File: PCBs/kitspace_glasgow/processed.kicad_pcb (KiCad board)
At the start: 4 copper layers, 80 x 49 mm, 267 parts, among them J1 USB_C_USB2.0, J10 AUX, J2 IDC-Header_2x10_P2.54mm, J3 IDC-Header_2x10_P2.54mm, J4 Conn_01x02, J5 PinHeader_2x22_P1.27mm, J6 Conn_01x08, J7 Conn_01x08, J8 Conn_01x08, J9 Conn_01x08, SW1 RST, U1 CY7C68013A-56LTX, U10 SN74LVC1T45DCKR, U11 SN74LVC1T45DCKR, U12 INA233, U13 DAC081C081CIMK, U14 TPS73101DBV, U15 TPD3S014, U16 SN74LVC1T45DCKR, U17 SN74LVC1T45DCKR, U18 SN74LVC1T45DCKR, U19 PCA6408APW, U2 CAT24M01X, U20 DAC081C081CIMK, U21 INA233, U22 SN74LVC1T45DCKR, U23 SN74LVC1T45DCKR, U24 SN74LVC1T45DCKR, U25 SN74LVC1T45DCKR, U26 SN74LVC1T45DCKR, U27 SN74LVC1T45DCKR, U28 SN74LVC1T45DCKR, U29 SN74LVC1T45DCKR, U3 BL24C256A-SFRC, U30 ICE40HX8K-BG121, U31 TPS73101DBV, U32 SN74LVC1T45DCKR, U36 TLV73312PQDRVR, U4 SN74LVC1T45DCKR, U5 PCA6408APW, U6 SN74LVC1T45DCKR, U7 APX811-40UG-7, U8 TLV75533PDRVR, U9 SN74LVC1T45DCKR, Y1 24M

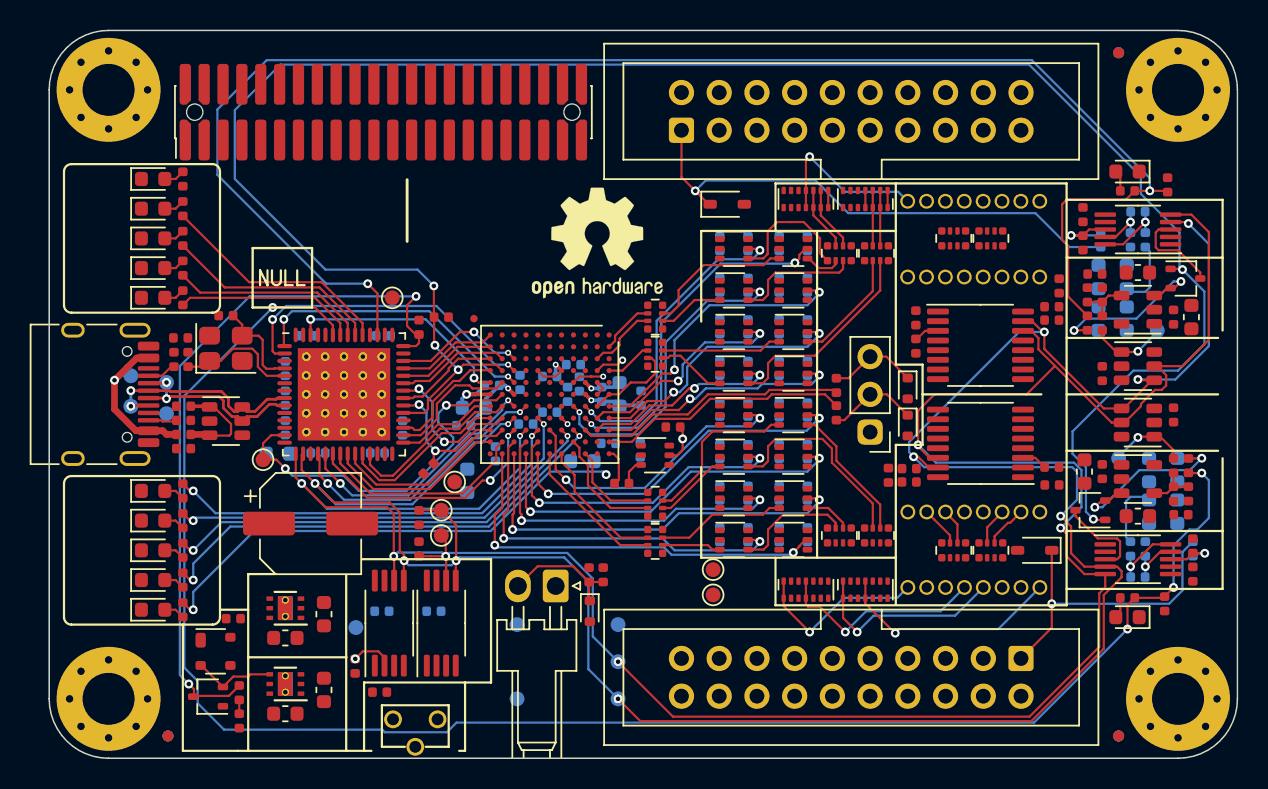
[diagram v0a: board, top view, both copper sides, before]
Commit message: recheck all circuits and clean up fill zone by rerouting the nets using freerouting and manually
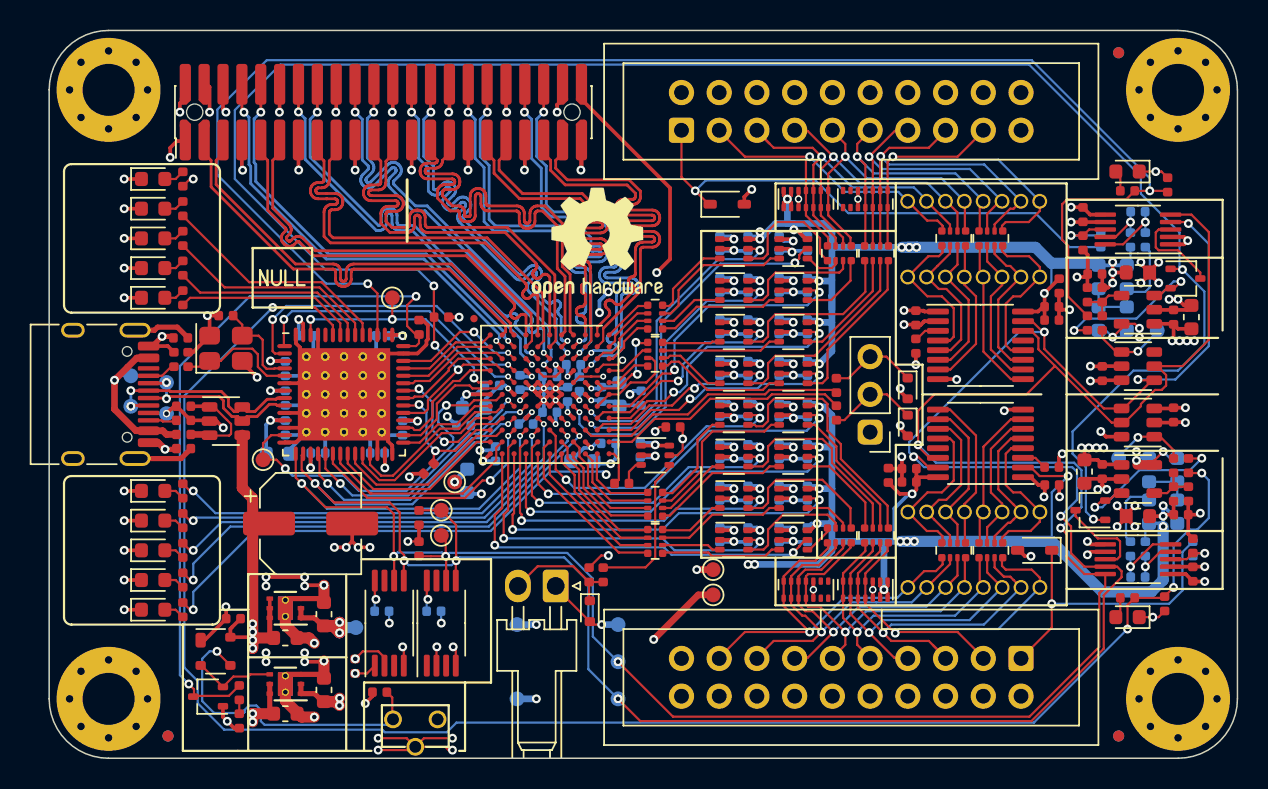
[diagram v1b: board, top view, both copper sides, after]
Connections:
- C1 pad 1: (no net) -> +3V3
- C1 pad 2: (no net) -> GND
- C10 pad 1: (no net) -> +3V3
- C10 pad 2: (no net) -> GND
- C11 pad 2: (no net) -> GND
- C12 pad 2: (no net) -> GND
- C13 pad 1: (no net) -> /SHLD
- C13 pad 2: (no net) -> GND
- C14 pad 1: (no net) -> +1V2
- C14 pad 2: (no net) -> GND
- C15 pad 1: (no net) -> +3V3
- C15 pad 2: (no net) -> GND
- C16 pad 1: (no net) -> +5V
- C16 pad 2: (no net) -> GND
- C17 pad 1: (no net) -> +3V3
- C17 pad 2: (no net) -> GND
- C18 pad 1: (no net) -> +1V2
- C18 pad 2: (no net) -> GND
- C19 pad 1: (no net) -> +3V3
- C19 pad 2: (no net) -> GND
- C2 pad 1: (no net) -> +3V3
- C2 pad 2: (no net) -> GND
- C20 pad 1: (no net) -> +3V3
- C20 pad 2: (no net) -> GND
- C21 pad 1: (no net) -> +3V3
- C21 pad 2: (no net) -> GND
- C22 pad 1: (no net) -> +3V3
- C22 pad 2: (no net) -> GND
- C23 pad 1: (no net) -> +3V3
- C23 pad 2: (no net) -> GND
- C24 pad 1: (no net) -> +1V2
- C24 pad 2: (no net) -> GND
- C25 pad 1: (no net) -> +1V2
- C25 pad 2: (no net) -> GND
- C26 pad 1: (no net) -> GND
- C26 pad 2: (no net) -> +5V
- C27 pad 1: (no net) -> +1V2
- C27 pad 2: (no net) -> GND
- C28 pad 1: (no net) -> +3V3
- C28 pad 2: (no net) -> GND
- C29 pad 1: (no net) -> /IO_Banks/VIOB
- C29 pad 2: (no net) -> GND
- C3 pad 1: (no net) -> +3V3
- C3 pad 2: (no net) -> GND
- C30 pad 1: (no net) -> +3V3
- C30 pad 2: (no net) -> GND
- C31 pad 1: (no net) -> +5V
- C31 pad 2: (no net) -> GND
- C32 pad 1: (no net) -> +3V3
- C32 pad 2: (no net) -> GND
- C33 pad 2: (no net) -> GND
- C34 pad 1: (no net) -> +3V3
- C34 pad 2: (no net) -> GND
- C35 pad 1: (no net) -> +3V3
- C35 pad 2: (no net) -> GND
- C36 pad 1: (no net) -> +3V3
- C36 pad 2: (no net) -> GND
- C37 pad 1: (no net) -> +3V3
- C37 pad 2: (no net) -> GND
- C38 pad 1: (no net) -> /IO_Banks/VIOA
- C38 pad 2: (no net) -> GND
- C39 pad 1: (no net) -> /IO_Banks/VIOA
- C39 pad 2: (no net) -> GND
- C4 pad 1: (no net) -> +3V3
- C4 pad 2: (no net) -> GND
- C40 pad 1: (no net) -> /IO_Banks/VIOA
- C40 pad 2: (no net) -> GND
- C41 pad 1: (no net) -> /IO_Banks/VIOA
- C41 pad 2: (no net) -> GND
- C42 pad 1: (no net) -> +3V3
- C42 pad 2: (no net) -> GND
- C43 pad 1: (no net) -> +3V3
- C43 pad 2: (no net) -> GND
- C45 pad 1: (no net) -> +5V
- C45 pad 2: (no net) -> GND
- C46 pad 1: (no net) -> /IO_Banks/VIOB
- C46 pad 2: (no net) -> GND
- C47 pad 1: (no net) -> +3V3
- C47 pad 2: (no net) -> GND
- C48 pad 1: (no net) -> +3V3
- C48 pad 2: (no net) -> GND
- C49 pad 1: (no net) -> /IO_Banks/VIOA
- C49 pad 2: (no net) -> GND
- C5 pad 1: (no net) -> +3V3
- C5 pad 2: (no net) -> GND
- C50 pad 1: (no net) -> /IO_Banks/VIOA
- C50 pad 2: (no net) -> GND
- C51 pad 1: (no net) -> /IO_Banks/VIOA
- C51 pad 2: (no net) -> GND
- C52 pad 1: (no net) -> /IO_Banks/VIOA
- C52 pad 2: (no net) -> GND
- C53 pad 1: (no net) -> /IO_Banks/VIOB
- C53 pad 2: (no net) -> GND
- C54 pad 1: (no net) -> /IO_Banks/VIOA
- C54 pad 2: (no net) -> GND
- C55 pad 1: (no net) -> +3V3
- C55 pad 2: (no net) -> GND
- C56 pad 1: (no net) -> +3V3
- C56 pad 2: (no net) -> GND
- C57 pad 1: (no net) -> /IO_Banks/VIOA
- C57 pad 2: (no net) -> GND
- C59 pad 1: (no net) -> +5V
- C59 pad 2: (no net) -> GND
- C6 pad 1: (no net) -> +3V3
- C6 pad 2: (no net) -> GND
- C60 pad 1: (no net) -> +3V3
- C60 pad 2: (no net) -> GND
- C61 pad 1: (no net) -> +3V3
- C61 pad 2: (no net) -> GND
- C62 pad 1: (no net) -> +3V3
- C62 pad 2: (no net) -> GND
- C63 pad 1: (no net) -> +3V3
- C63 pad 2: (no net) -> GND
- C64 pad 1: (no net) -> /IO_Banks/VIOB
- C64 pad 2: (no net) -> GND
- C65 pad 1: (no net) -> /IO_Banks/VIOB
- C65 pad 2: (no net) -> GND
- C66 pad 1: (no net) -> /IO_Banks/VIOB
- C66 pad 2: (no net) -> GND
- C67 pad 1: (no net) -> /IO_Banks/VIOB
- C67 pad 2: (no net) -> GND
- C68 pad 1: (no net) -> +3V3
- C68 pad 2: (no net) -> GND
- C69 pad 1: (no net) -> +3V3
- C69 pad 2: (no net) -> GND
- C7 pad 1: (no net) -> +3V3
- C7 pad 2: (no net) -> GND
- C70 pad 1: (no net) -> +3V3
- C70 pad 2: (no net) -> GND
- C71 pad 1: (no net) -> +3V3
- C71 pad 2: (no net) -> GND
- C72 pad 1: (no net) -> /IO_Banks/VIOB
- C72 pad 2: (no net) -> GND
- C73 pad 1: (no net) -> /IO_Banks/VIOB
- C73 pad 2: (no net) -> GND
- C74 pad 1: (no net) -> /IO_Banks/VIOB
- C74 pad 2: (no net) -> GND
- C75 pad 1: (no net) -> /IO_Banks/VIOB
- C75 pad 2: (no net) -> GND
- C77 pad 1: (no net) -> +1V2
- C77 pad 2: (no net) -> GND
- C8 pad 2: (no net) -> GND
- C81 pad 1: (no net) -> +3V3
- C81 pad 2: (no net) -> GND
- C82 pad 1: (no net) -> +5V
- C82 pad 2: (no net) -> GND
- C83 pad 1: (no net) -> /IO_Banks/VIOA
- C83 pad 2: (no net) -> GND
- C84 pad 1: (no net) -> +3V3
- C84 pad 2: (no net) -> GND
- C85 pad 1: (no net) -> +3V3
- C85 pad 2: (no net) -> GND
- C86 pad 1: (no net) -> GND
- C86 pad 2: (no net) -> +5V
- C87 pad 1: (no net) -> +5V
- C87 pad 2: (no net) -> GND
- C88 pad 2: (no net) -> GND
- C89 pad 1: (no net) -> /~MR
- C89 pad 2: (no net) -> GND
- C9 pad 1: (no net) -> +3V3
- C9 pad 2: (no net) -> GND
- C90 pad 1: (no net) -> GND
- C91 pad 1: (no net) -> GND
- D1 pad 1: (no net) -> GND
- D10 pad 1: (no net) -> GND
- D11 pad 2: (no net) -> GND
- D12 pad 2: (no net) -> GND
- D13 pad 2: (no net) -> GND
- D14 pad 1: (no net) -> GND
- D15 pad 1: (no net) -> GND
- D16 pad 2: (no net) -> GND
- D17 pad 2: (no net) -> GND
- D2 pad 1: (no net) -> GND
- D20 pad 10: (no net) -> GND
- D20 pad 12: (no net) -> /IO_Banks/IO_Buffer_B/Z1
- D20 pad 13: (no net) -> /IO_Banks/IO_Buffer_B/Z2
- D20 pad 2: (no net) -> /IO_Banks/IO_Buffer_B/Z2
- D20 pad 3: (no net) -> /IO_Banks/IO_Buffer_B/Z1
- D20 pad 5: (no net) -> GND
- D20 pad 6: (no net) -> /IO_Banks/VIOB
- D20 pad 7: (no net) -> /IO_Banks/VIOB
- D20 pad 8: (no net) -> /IO_Banks/VIOB
- D20 pad 9: (no net) -> /IO_Banks/VIOB
- D21 pad 10: (no net) -> GND
- D21 pad 12: (no net) -> /IO_Banks/IO_Buffer_B/Z5
- D21 pad 13: (no net) -> /IO_Banks/IO_Buffer_B/Z6
- D21 pad 2: (no net) -> /IO_Banks/IO_Buffer_B/Z6
- D21 pad 3: (no net) -> /IO_Banks/IO_Buffer_B/Z5
- D21 pad 5: (no net) -> GND
- D22 pad 10: (no net) -> GND
- D22 pad 5: (no net) -> GND
- D22 pad 6: (no net) -> /IO_Banks/VIOA
- D22 pad 7: (no net) -> /IO_Banks/VIOA
- D22 pad 8: (no net) -> /IO_Banks/VIOA
- D22 pad 9: (no net) -> /IO_Banks/VIOA
- D23 pad 10: (no net) -> GND
- D23 pad 5: (no net) -> GND
- D24 pad 1: (no net) -> +3V3
- D3 pad 1: (no net) -> GND
- D4 pad 1: (no net) -> GND
- D5 pad 1: (no net) -> GND
- D6 pad 1: (no net) -> GND
- D7 pad 1: (no net) -> GND
- D8 pad 1: (no net) -> GND
- D9 pad 1: (no net) -> GND
- J1 pad A1: (no net) -> GND
- J1 pad A12: (no net) -> GND
- J1 pad B1: (no net) -> GND
- J1 pad B12: (no net) -> GND
- J1 pad S1: (no net) -> /SHLD
- J10 pad 1: (no net) -> GND
- J2 pad 10: (no net) -> GND
- J2 pad 11: (no net) -> /IO_Banks/IO_Buffer_A/Z4
- J2 pad 12: (no net) -> GND
- J2 pad 13: (no net) -> /IO_Banks/IO_Buffer_A/Z5
- J2 pad 14: (no net) -> GND
- J2 pad 15: (no net) -> /IO_Banks/IO_Buffer_A/Z6
- J2 pad 16: (no net) -> GND
- J2 pad 17: (no net) -> /IO_Banks/IO_Buffer_A/Z7
- J2 pad 18: (no net) -> GND
- J2 pad 2: (no net) -> /IO_Banks/VIOA
- J2 pad 3: (no net) -> /IO_Banks/IO_Buffer_A/Z0
- J2 pad 4: (no net) -> GND
- J2 pad 5: (no net) -> /IO_Banks/IO_Buffer_A/Z1
- J2 pad 6: (no net) -> GND
- J2 pad 7: (no net) -> /IO_Banks/IO_Buffer_A/Z2
- J2 pad 8: (no net) -> GND
- J2 pad 9: (no net) -> /IO_Banks/IO_Buffer_A/Z3
- J3 pad 10: (no net) -> GND
- J3 pad 11: (no net) -> /IO_Banks/IO_Buffer_B/Z4
- J3 pad 12: (no net) -> GND
- J3 pad 13: (no net) -> /IO_Banks/IO_Buffer_B/Z5
- J3 pad 14: (no net) -> GND
- J3 pad 15: (no net) -> /IO_Banks/IO_Buffer_B/Z6
- J3 pad 16: (no net) -> GND
- J3 pad 17: (no net) -> /IO_Banks/IO_Buffer_B/Z7
- J3 pad 18: (no net) -> GND
- J3 pad 2: (no net) -> /IO_Banks/VIOB
- J3 pad 3: (no net) -> /IO_Banks/IO_Buffer_B/Z0
- J3 pad 4: (no net) -> GND
- J3 pad 5: (no net) -> /IO_Banks/IO_Buffer_B/Z1
- J3 pad 6: (no net) -> GND
- J3 pad 7: (no net) -> /IO_Banks/IO_Buffer_B/Z2
- J3 pad 8: (no net) -> GND
- J3 pad 9: (no net) -> /IO_Banks/IO_Buffer_B/Z3
- J4 pad 1: (no net) -> GND
- J5 pad 1: (no net) -> GND
- J5 pad 10: (no net) -> /IO_Banks/Z12_N
- J5 pad 11: (no net) -> /IO_Banks/Z10_N
- J5 pad 12: (no net) -> GND
- J5 pad 13: (no net) -> GND
- J5 pad 14: (no net) -> /IO_Banks/Z9_N
- J5 pad 15: (no net) -> /IO_Banks/Z8_P
- J5 pad 16: (no net) -> /IO_Banks/Z9_P
- J5 pad 17: (no net) -> /IO_Banks/Z8_N
- J5 pad 18: (no net) -> GND
- J5 pad 19: (no net) -> GND
- J5 pad 2: (no net) -> +3V3
- J5 pad 20: (no net) -> /IO_Banks/Z7_N
- J5 pad 21: (no net) -> /IO_Banks/Z6_P
- J5 pad 22: (no net) -> /IO_Banks/Z7_P
- J5 pad 23: (no net) -> /IO_Banks/Z6_N
- J5 pad 24: (no net) -> GND
- J5 pad 25: (no net) -> GND
- J5 pad 26: (no net) -> /IO_Banks/Z5_N
- J5 pad 27: (no net) -> /IO_Banks/Z3_P
- J5 pad 28: (no net) -> /IO_Banks/Z5_P
- J5 pad 29: (no net) -> /IO_Banks/Z3_N
- J5 pad 3: (no net) -> /IO_Banks/Z11_N
- J5 pad 30: (no net) -> GND
- J5 pad 31: (no net) -> GND
- J5 pad 32: (no net) -> /IO_Banks/Z4_P
- J5 pad 33: (no net) -> /IO_Banks/Z2_N
- J5 pad 34: (no net) -> /IO_Banks/Z4_N
- J5 pad 35: (no net) -> /IO_Banks/Z2_P
- J5 pad 36: (no net) -> GND
- J5 pad 37: (no net) -> GND
- J5 pad 38: (no net) -> /IO_Banks/Z1_N
- J5 pad 39: (no net) -> /IO_Banks/Z0_P
- J5 pad 4: (no net) -> GND
- J5 pad 40: (no net) -> /IO_Banks/Z1_P
- J5 pad 41: (no net) -> /IO_Banks/Z0_N
- J5 pad 42: (no net) -> GND
- J5 pad 43: (no net) -> GND
- J5 pad 44: (no net) -> /IO_Banks/VIO_AUX
- J5 pad 5: (no net) -> /IO_Banks/Z11_P
- J5 pad 6: (no net) -> GND
- J5 pad 7: (no net) -> GND
- J5 pad 8: (no net) -> /IO_Banks/Z12_P
- J5 pad 9: (no net) -> /IO_Banks/Z10_P
- J6 pad 2: (no net) -> /IO_Banks/IO_Buffer_B/Z1
- J6 pad 3: (no net) -> /IO_Banks/IO_Buffer_B/Z2
- J6 pad 6: (no net) -> /IO_Banks/IO_Buffer_B/Z5
- J6 pad 7: (no net) -> /IO_Banks/IO_Buffer_B/Z6
- J7 pad 1: (no net) -> /IO_Banks/IO_Buffer_B/P0
- J7 pad 4: (no net) -> /IO_Banks/IO_Buffer_B/P3
- J7 pad 5: (no net) -> /IO_Banks/IO_Buffer_B/P4
- J7 pad 8: (no net) -> /IO_Banks/IO_Buffer_B/P7
- J8 pad 2: (no net) -> /IO_Banks/IO_Buffer_A/Z1
- J8 pad 3: (no net) -> /IO_Banks/IO_Buffer_A/Z2
- J8 pad 4: (no net) -> /IO_Banks/IO_Buffer_A/Z3
- J8 pad 5: (no net) -> /IO_Banks/IO_Buffer_A/Z4
- J8 pad 6: (no net) -> /IO_Banks/IO_Buffer_A/Z5
- J8 pad 7: (no net) -> /IO_Banks/IO_Buffer_A/Z6
- J8 pad 8: (no net) -> /IO_Banks/IO_Buffer_A/Z7
- J9 pad 1: (no net) -> /IO_Banks/IO_Buffer_A/P0
- J9 pad 2: (no net) -> /IO_Banks/IO_Buffer_A/P1
- J9 pad 3: (no net) -> /IO_Banks/IO_Buffer_A/P2
- J9 pad 4: (no net) -> /IO_Banks/IO_Buffer_A/P3
- J9 pad 5: (no net) -> /IO_Banks/IO_Buffer_A/P4
- J9 pad 6: (no net) -> /IO_Banks/IO_Buffer_A/P5
- J9 pad 7: (no net) -> /IO_Banks/IO_Buffer_A/P6
- J9 pad 8: (no net) -> /IO_Banks/IO_Buffer_A/P7
- MK1 pad 1: (no net) -> GND
- MK2 pad 1: (no net) -> GND
- MK3 pad 1: (no net) -> GND
- MK4 pad 1: (no net) -> GND
- R1 pad 2: (no net) -> +3V3
- R10 pad 2: (no net) -> GND
- R12 pad 1: (no net) -> +3V3
- R17 pad 2: (no net) -> +3V3
- R18 pad 2: (no net) -> GND
- R19 pad 2: (no net) -> GND
- R2 pad 2: (no net) -> +3V3
- R25 pad 1: (no net) -> /IO_Banks/VIOB
- R28 pad 2: (no net) -> /IO_Banks/VIOB
- R29 pad 1: (no net) -> GND
- R3 pad 1: (no net) -> /SHLD
- R3 pad 2: (no net) -> GND
- R31 pad 2: (no net) -> +1V2
- R32 pad 2: (no net) -> +1V2
- R34 pad 2: (no net) -> /IO_Banks/VIOA
- R35 pad 1: (no net) -> GND
- R36 pad 2: (no net) -> +3V3
- R37 pad 2: (no net) -> +3V3
- R38 pad 2: (no net) -> Net-(R38-Pad2)
- R4 pad 1: (no net) -> +3V3
- R40 pad 2: (no net) -> +3V3
- R41 pad 1: (no net) -> GND
- R41 pad 2: (no net) -> /IO_Banks/VIOB
- R42 pad 1: (no net) -> GND
- R42 pad 2: (no net) -> /IO_Banks/VIOA
- R44 pad 2: (no net) -> +3V3
- R48 pad 2: (no net) -> /IO_Banks/VIOB
- R49 pad 2: (no net) -> /IO_Banks/VIOA
- R50 pad 1: (no net) -> /IO_Banks/IO_Buffer_B/ISNS_H
- R50 pad 2: (no net) -> /IO_Banks/VIOB
- R51 pad 1: (no net) -> /IO_Banks/IO_Buffer_A/ISNS_H
- R51 pad 2: (no net) -> /IO_Banks/VIOA
- R52 pad 1: (no net) -> GND
- R53 pad 1: (no net) -> GND
- R54 pad 1: (no net) -> /IO_Banks/VIOA
- R56 pad 1: (no net) -> Net-(R56-Pad1)
- R56 pad 2: (no net) -> /IO_Banks/IO_Buffer_A/ISNS_H
- R57 pad 1: (no net) -> GND
- R57 pad 2: (no net) -> /IO_Banks/VIOB
- R58 pad 1: (no net) -> GND
- R58 pad 2: (no net) -> /IO_Banks/VIOA
- R6 pad 1: (no net) -> Net-(R6-Pad1)
- R6 pad 2: (no net) -> /IO_Banks/IO_Buffer_B/ISNS_H
- R7 pad 1: (no net) -> Net-(R6-Pad1)
- R7 pad 2: (no net) -> /IO_Banks/IO_Buffer_B/ISNS_H
- R8 pad 1: (no net) -> Net-(R56-Pad1)
- R8 pad 2: (no net) -> /IO_Banks/IO_Buffer_A/ISNS_H
- R9 pad 1: (no net) -> GND
- RN1 pad 1: (no net) -> /IO_Banks/QB0
- RN1 pad 4: (no net) -> /IO_Banks/QB3
- RN1 pad 5: (no net) -> Net-(RN1-Pad5)
- RN1 pad 8: (no net) -> /IO_Banks/IO_Buffer_B/X0
- RN10 pad 1: (no net) -> /IO_Banks/IO_Buffer_A/Y4
- RN10 pad 4: (no net) -> /IO_Banks/IO_Buffer_A/Y7
- RN10 pad 5: (no net) -> /IO_Banks/IO_Buffer_A/Z7
- RN10 pad 8: (no net) -> /IO_Banks/IO_Buffer_A/Z4
- RN11 pad 1: (no net) -> /IO_Banks/IO_Buffer_A/Z3
- RN11 pad 2: (no net) -> /IO_Banks/IO_Buffer_A/Z2
- RN11 pad 3: (no net) -> /IO_Banks/IO_Buffer_A/Z1
- RN11 pad 4: (no net) -> /IO_Banks/IO_Buffer_A/Z0
- RN11 pad 5: (no net) -> /IO_Banks/IO_Buffer_A/P0
- RN11 pad 6: (no net) -> /IO_Banks/IO_Buffer_A/P1
- RN11 pad 7: (no net) -> /IO_Banks/IO_Buffer_A/P2
- RN11 pad 8: (no net) -> /IO_Banks/IO_Buffer_A/P3
- RN12 pad 1: (no net) -> /IO_Banks/IO_Buffer_A/Z7
- RN12 pad 2: (no net) -> /IO_Banks/IO_Buffer_A/Z6
- RN12 pad 3: (no net) -> /IO_Banks/IO_Buffer_A/Z5
- RN12 pad 4: (no net) -> /IO_Banks/IO_Buffer_A/Z4
- RN12 pad 5: (no net) -> /IO_Banks/IO_Buffer_A/P4
- RN12 pad 6: (no net) -> /IO_Banks/IO_Buffer_A/P5
- RN12 pad 7: (no net) -> /IO_Banks/IO_Buffer_A/P6
- RN12 pad 8: (no net) -> /IO_Banks/IO_Buffer_A/P7
- RN2 pad 1: (no net) -> /IO_Banks/QB4
- RN2 pad 4: (no net) -> /IO_Banks/QB7
- RN2 pad 5: (no net) -> Net-(RN2-Pad5)
- RN2 pad 8: (no net) -> Net-(RN2-Pad8)
- RN3 pad 1: (no net) -> /IO_Banks/IO_Buffer_B/Y0
- RN3 pad 4: (no net) -> /IO_Banks/IO_Buffer_B/Y3
- RN3 pad 5: (no net) -> /IO_Banks/IO_Buffer_B/Z3
- RN3 pad 6: (no net) -> /IO_Banks/IO_Buffer_B/Z2
- RN3 pad 7: (no net) -> /IO_Banks/IO_Buffer_B/Z1
- RN3 pad 8: (no net) -> /IO_Banks/IO_Buffer_B/Z0
- RN4 pad 1: (no net) -> /IO_Banks/IO_Buffer_B/Y4
- RN4 pad 4: (no net) -> /IO_Banks/IO_Buffer_B/Y7
- RN4 pad 5: (no net) -> /IO_Banks/IO_Buffer_B/Z7
- RN4 pad 6: (no net) -> /IO_Banks/IO_Buffer_B/Z6
- RN4 pad 7: (no net) -> /IO_Banks/IO_Buffer_B/Z5
- RN4 pad 8: (no net) -> /IO_Banks/IO_Buffer_B/Z4
- RN5 pad 1: (no net) -> /IO_Banks/IO_Buffer_B/Z3
- RN5 pad 2: (no net) -> /IO_Banks/IO_Buffer_B/Z2
- RN5 pad 3: (no net) -> /IO_Banks/IO_Buffer_B/Z1
- RN5 pad 4: (no net) -> /IO_Banks/IO_Buffer_B/Z0
- RN5 pad 5: (no net) -> /IO_Banks/IO_Buffer_B/P0
- RN5 pad 8: (no net) -> /IO_Banks/IO_Buffer_B/P3
- RN6 pad 1: (no net) -> /IO_Banks/IO_Buffer_B/Z7
- RN6 pad 2: (no net) -> /IO_Banks/IO_Buffer_B/Z6
- RN6 pad 3: (no net) -> /IO_Banks/IO_Buffer_B/Z5
- RN6 pad 4: (no net) -> /IO_Banks/IO_Buffer_B/Z4
- RN6 pad 5: (no net) -> /IO_Banks/IO_Buffer_B/P4
- RN6 pad 8: (no net) -> /IO_Banks/IO_Buffer_B/P7
- RN7 pad 1: (no net) -> /IO_Banks/QA0
- RN7 pad 4: (no net) -> /IO_Banks/QA3
- RN7 pad 5: (no net) -> Net-(RN7-Pad5)
- RN7 pad 8: (no net) -> /IO_Banks/IO_Buffer_A/X0
- RN8 pad 1: (no net) -> /IO_Banks/QA4
- RN8 pad 4: (no net) -> /IO_Banks/QA7
- RN8 pad 5: (no net) -> Net-(RN8-Pad5)
- RN8 pad 8: (no net) -> Net-(RN8-Pad8)
- RN9 pad 4: (no net) -> /IO_Banks/IO_Buffer_A/Y3
- RN9 pad 5: (no net) -> /IO_Banks/IO_Buffer_A/Z3
- RN9 pad 8: (no net) -> /IO_Banks/IO_Buffer_A/Z0
- SW1 pad 1: (no net) -> GND
- SW1 pad 2: (no net) -> /~MR
- SW1 pad 3: (no net) -> /SWSH
- TP1 pad 1: (no net) -> +5V
- TP12 pad 1: (no net) -> GND
- TP14 pad 1: (no net) -> GND
- TP17 pad 1: (no net) -> +1V2
- TP2 pad 1: (no net) -> +1V2
- TP3 pad 1: (no net) -> +3V3
- TP6 pad 1: (no net) -> /CLKREF
- TP8 pad 1: (no net) -> +5V
- TP9 pad 1: (no net) -> +3V3
- U1 pad 10: (no net) -> GND
- U1 pad 11: (no net) -> +3V3
- U1 pad 12: (no net) -> GND
- U1 pad 14: (no net) -> GND
- U1 pad 17: (no net) -> +3V3
- U1 pad 26: (no net) -> GND
- U1 pad 27: (no net) -> +3V3
- U1 pad 28: (no net) -> GND
- U1 pad 3: (no net) -> +3V3
- U1 pad 32: (no net) -> +3V3
- U1 pad 41: (no net) -> GND
- U1 pad 43: (no net) -> +3V3
- U1 pad 44: (no net) -> +3V3
- U1 pad 53: (no net) -> GND
- U1 pad 55: (no net) -> +3V3
- U1 pad 56: (no net) -> GND
- U1 pad 57: (no net) -> GND
- U1 pad 6: (no net) -> GND
- U1 pad 7: (no net) -> +3V3
- U10 pad 1: (no net) -> +3V3
- U10 pad 2: (no net) -> GND
- U10 pad 6: (no net) -> /IO_Banks/VIOA
- U11 pad 1: (no net) -> +3V3
- U11 pad 2: (no net) -> GND
- U11 pad 6: (no net) -> /IO_Banks/VIOA
- U12 pad 1: (no net) -> GND
- U12 pad 2: (no net) -> +3V3
- U12 pad 6: (no net) -> +3V3
- U12 pad 7: (no net) -> GND
- U13 pad 2: (no net) -> +3V3
- U13 pad 3: (no net) -> GND
- U13 pad 6: (no net) -> GND
- U14 pad 1: (no net) -> +5V
- U14 pad 2: (no net) -> GND
- U14 pad 5: (no net) -> Net-(R6-Pad1)
- U15 pad 2: (no net) -> GND
- U15 pad 4: (no net) -> +5V
- U16 pad 1: (no net) -> +3V3
- U16 pad 2: (no net) -> GND
- U16 pad 3: (no net) -> Net-(RN7-Pad5)
- U16 pad 4: (no net) -> /IO_Banks/IO_Buffer_A/Y3
- U16 pad 6: (no net) -> /IO_Banks/VIOA
- U17 pad 1: (no net) -> +3V3
- U17 pad 2: (no net) -> GND
- U17 pad 6: (no net) -> /IO_Banks/VIOA
- U18 pad 1: (no net) -> +3V3
- U18 pad 2: (no net) -> GND
- U18 pad 3: (no net) -> Net-(RN8-Pad5)
- U18 pad 4: (no net) -> /IO_Banks/IO_Buffer_A/Y7
- U18 pad 6: (no net) -> /IO_Banks/VIOA
- U19 pad 1: (no net) -> +3V3
- U19 pad 10: (no net) -> /IO_Banks/IO_Buffer_A/P5
- U19 pad 11: (no net) -> /IO_Banks/IO_Buffer_A/P6
- U19 pad 12: (no net) -> /IO_Banks/IO_Buffer_A/P7
- U19 pad 16: (no net) -> /IO_Banks/VIOA
- U19 pad 2: (no net) -> GND
- U19 pad 4: (no net) -> /IO_Banks/IO_Buffer_A/P0
- U19 pad 5: (no net) -> /IO_Banks/IO_Buffer_A/P1
- U19 pad 6: (no net) -> /IO_Banks/IO_Buffer_A/P2
- U19 pad 7: (no net) -> /IO_Banks/IO_Buffer_A/P3
- U19 pad 8: (no net) -> GND
- U19 pad 9: (no net) -> /IO_Banks/IO_Buffer_A/P4
- U2 pad 2: (no net) -> +3V3
- U2 pad 4: (no net) -> GND
- U2 pad 8: (no net) -> +3V3
- U20 pad 2: (no net) -> +3V3
- U20 pad 3: (no net) -> GND
- U21 pad 1: (no net) -> GND
- U21 pad 2: (no net) -> GND
- U21 pad 6: (no net) -> +3V3
- U21 pad 7: (no net) -> GND
- U22 pad 1: (no net) -> +3V3
- U22 pad 2: (no net) -> GND
- U22 pad 3: (no net) -> /IO_Banks/IO_Buffer_B/X0
- U22 pad 4: (no net) -> /IO_Banks/IO_Buffer_B/Y0
- U22 pad 6: (no net) -> /IO_Banks/VIOB
- U23 pad 1: (no net) -> +3V3
- U23 pad 2: (no net) -> GND
- U23 pad 6: (no net) -> /IO_Banks/VIOB
- U24 pad 1: (no net) -> +3V3
- U24 pad 2: (no net) -> GND
- U24 pad 3: (no net) -> Net-(RN2-Pad8)
- U24 pad 4: (no net) -> /IO_Banks/IO_Buffer_B/Y4
- U24 pad 6: (no net) -> /IO_Banks/VIOB
- U25 pad 1: (no net) -> +3V3
- U25 pad 2: (no net) -> GND
- U25 pad 6: (no net) -> /IO_Banks/VIOB
- U26 pad 1: (no net) -> +3V3
- U26 pad 2: (no net) -> GND
- U26 pad 6: (no net) -> /IO_Banks/VIOB
- U27 pad 1: (no net) -> +3V3
- U27 pad 2: (no net) -> GND
- U27 pad 3: (no net) -> Net-(RN1-Pad5)
- U27 pad 4: (no net) -> /IO_Banks/IO_Buffer_B/Y3
- U27 pad 6: (no net) -> /IO_Banks/VIOB
- U28 pad 1: (no net) -> +3V3
- U28 pad 2: (no net) -> GND
- U28 pad 6: (no net) -> /IO_Banks/VIOB
- U29 pad 1: (no net) -> +3V3
- U29 pad 2: (no net) -> GND
- U29 pad 3: (no net) -> Net-(RN2-Pad5)
- U29 pad 4: (no net) -> /IO_Banks/IO_Buffer_B/Y7
- U29 pad 6: (no net) -> /IO_Banks/VIOB
- U3 pad 1: (no net) -> +3V3
- U3 pad 4: (no net) -> GND
- U3 pad 8: (no net) -> +3V3
- U30 pad A1: (no net) -> /IO_Banks/QA0
- U30 pad A3: (no net) -> /IO_Banks/QA3
- U30 pad A5: (no net) -> /IO_Banks/QA7
- U30 pad B1: (no net) -> /IO_Banks/Z0_P
- U30 pad B11: (no net) -> /IO_Banks/QB0
- U30 pad B2: (no net) -> /IO_Banks/Z0_N
- U30 pad C1: (no net) -> /IO_Banks/Z2_N
- U30 pad C10: (no net) -> +3V3
- U30 pad C2: (no net) -> /IO_Banks/Z2_P
- U30 pad C3: (no net) -> /IO_Banks/Z1_N
- U30 pad C4: (no net) -> /IO_Banks/Z1_P
- U30 pad D1: (no net) -> /IO_Banks/Z3_N
- U30 pad D11: (no net) -> /IO_Banks/QB3
- U30 pad D2: (no net) -> /IO_Banks/Z4_P
- U30 pad D3: (no net) -> /IO_Banks/Z4_N
- U30 pad D4: (no net) -> +1V2
- U30 pad D6: (no net) -> +3V3
- U30 pad D8: (no net) -> +1V2
- U30 pad E1: (no net) -> /IO_Banks/Z3_P
- U30 pad E10: (no net) -> /IO_Banks/QB4
- U30 pad E2: (no net) -> /IO_Banks/Z5_P
- U30 pad E3: (no net) -> /IO_Banks/Z5_N
- U30 pad E5: (no net) -> GND
- U30 pad E6: (no net) -> GND
- U30 pad E7: (no net) -> GND
- U30 pad F1: (no net) -> /IO_Banks/Z6_P
- U30 pad F10: (no net) -> /IO_Banks/QB7
- U30 pad F2: (no net) -> /IO_Banks/Z6_N
- U30 pad F3: (no net) -> /IO_Banks/Z7_N
- U30 pad F4: (no net) -> /IO_Banks/Z7_P
- U30 pad F5: (no net) -> GND
- U30 pad F6: (no net) -> GND
- U30 pad F7: (no net) -> GND
- U30 pad F8: (no net) -> +3V3
- U30 pad G1: (no net) -> /IO_Banks/Z8_P
- U30 pad G2: (no net) -> /IO_Banks/Z8_N
- U30 pad G3: (no net) -> /IO_Banks/Z9_P
- U30 pad G5: (no net) -> GND
- U30 pad G6: (no net) -> GND
- U30 pad G7: (no net) -> GND
- U30 pad H1: (no net) -> /IO_Banks/Z10_P
- U30 pad H2: (no net) -> /IO_Banks/Z10_N
- U30 pad H3: (no net) -> /IO_Banks/Z9_N
- U30 pad H4: (no net) -> +1V2
- U30 pad H5: (no net) -> GND
- U30 pad H6: (no net) -> +3V3
- U30 pad H8: (no net) -> +1V2
- U30 pad J1: (no net) -> /IO_Banks/Z11_P
- U30 pad J2: (no net) -> /IO_Banks/Z12_N
- U30 pad K1: (no net) -> /IO_Banks/Z11_N
- U30 pad K2: (no net) -> /IO_Banks/Z12_P
- U30 pad L11: (no net) -> +3V3
- U31 pad 1: (no net) -> +5V
- U31 pad 2: (no net) -> GND
- U31 pad 5: (no net) -> Net-(R56-Pad1)
- U32 pad 1: (no net) -> +3V3
- U32 pad 2: (no net) -> GND
- U32 pad 4: (no net) -> Net-(R38-Pad2)
- U32 pad 6: (no net) -> +3V3
- U36 pad 1: (no net) -> +1V2
- U36 pad 2: (no net) -> +1V2
- U36 pad 3: (no net) -> GND
- U36 pad 4: (no net) -> +5V
- U36 pad 5: (no net) -> +5V
- U36 pad 6: (no net) -> +5V
- U36 pad 7: (no net) -> GND
- U4 pad 1: (no net) -> +3V3
- U4 pad 2: (no net) -> GND
- U4 pad 3: (no net) -> /IO_Banks/IO_Buffer_A/X0
- U4 pad 6: (no net) -> /IO_Banks/VIOA
- U5 pad 1: (no net) -> +3V3
- U5 pad 10: (no net) -> /IO_Banks/IO_Buffer_B/P5
- U5 pad 11: (no net) -> /IO_Banks/IO_Buffer_B/P6
- U5 pad 12: (no net) -> /IO_Banks/IO_Buffer_B/P7
- U5 pad 16: (no net) -> /IO_Banks/VIOB
- U5 pad 2: (no net) -> /IO_Banks/VIOB
- U5 pad 4: (no net) -> /IO_Banks/IO_Buffer_B/P0
- U5 pad 5: (no net) -> /IO_Banks/IO_Buffer_B/P1
- U5 pad 6: (no net) -> /IO_Banks/IO_Buffer_B/P2
- U5 pad 7: (no net) -> /IO_Banks/IO_Buffer_B/P3
- U5 pad 8: (no net) -> GND
- U5 pad 9: (no net) -> /IO_Banks/IO_Buffer_B/P4
- U6 pad 1: (no net) -> +3V3
- U6 pad 2: (no net) -> GND
- U6 pad 6: (no net) -> /IO_Banks/VIOA
- U7 pad 1: (no net) -> GND
- U7 pad 3: (no net) -> /~MR
- U7 pad 4: (no net) -> +5V
- U8 pad 1: (no net) -> +3V3
- U8 pad 2: (no net) -> +3V3
- U8 pad 3: (no net) -> GND
- U8 pad 5: (no net) -> +5V
- U8 pad 6: (no net) -> +5V
- U8 pad 7: (no net) -> GND
- U9 pad 1: (no net) -> +3V3
- U9 pad 2: (no net) -> GND
- U9 pad 3: (no net) -> Net-(RN8-Pad8)
- U9 pad 4: (no net) -> /IO_Banks/IO_Buffer_A/Y4
- U9 pad 6: (no net) -> /IO_Banks/VIOA
- Y1 pad 2: (no net) -> GND
- Y1 pad 4: (no net) -> GND
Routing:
- net GND: track 0.00 -> 766.6 mm, vias 0 -> 119
- net +3V3: track 0.00 -> 406.8 mm, vias 0 -> 53
- net +5V: track 0.00 -> 147.4 mm, vias 0 -> 16
- net /IO_Banks/VIOB: track 0.00 -> 126.0 mm, vias 0 -> 19
- net /IO_Banks/VIOA: track 0.00 -> 104.6 mm, vias 0 -> 17
- net +1V2: track 0.00 -> 58.0 mm, vias 0 -> 9
- net /IO_Banks/Z0_P: track 0.00 -> 29.6 mm
- net /IO_Banks/Z11_N: track 0.00 -> 29.4 mm
- net /IO_Banks/Z11_P: track 0.00 -> 29.4 mm
- net /IO_Banks/Z7_N: track 0.00 -> 29.3 mm, vias 0 -> 2
- net /IO_Banks/Z7_P: track 0.00 -> 29.3 mm, vias 0 -> 2
- net /IO_Banks/Z9_P: track 0.00 -> 29.2 mm, vias 0 -> 2
- net /IO_Banks/Z9_N: track 0.00 -> 29.2 mm, vias 0 -> 2
- net /IO_Banks/Z2_N: track 0.00 -> 29.1 mm
- net /IO_Banks/Z12_P: track 0.00 -> 29.1 mm, vias 0 -> 2
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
